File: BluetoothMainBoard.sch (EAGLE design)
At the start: 33 parts, among them IC1 MCP73831, J1 J_USB_MICROAB_HIROSE_ZX62-AB-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, U1 MAX921MSA/PR

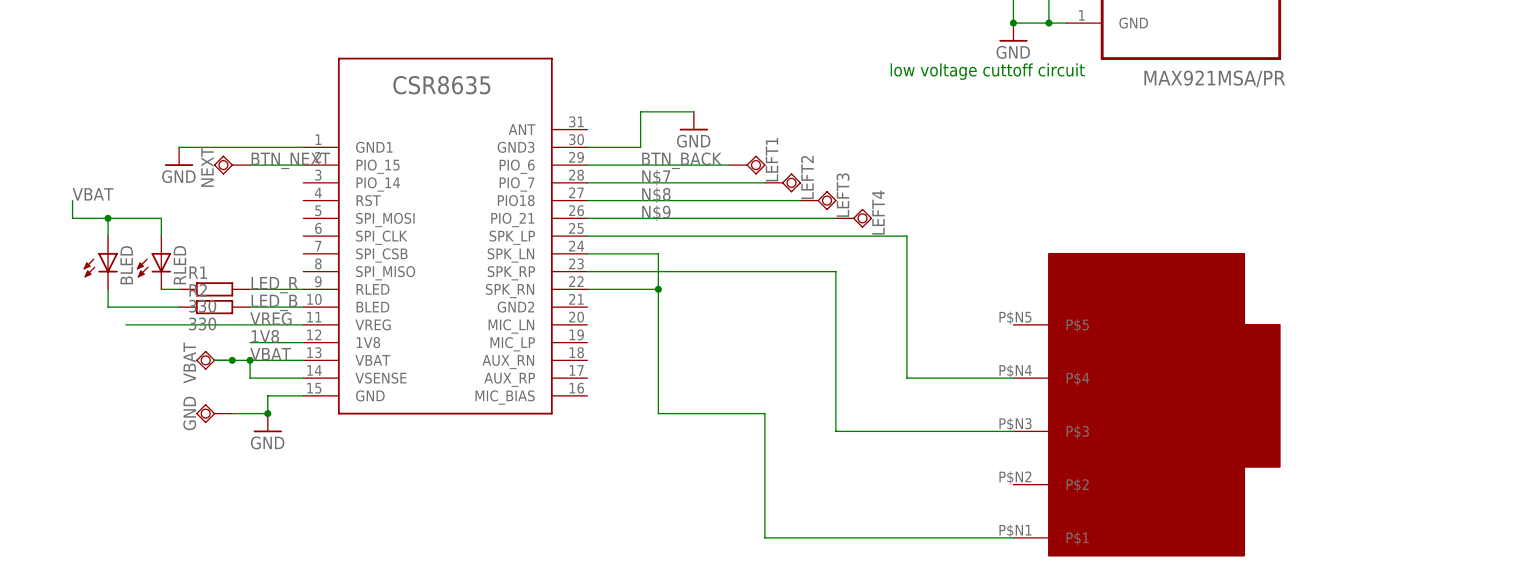
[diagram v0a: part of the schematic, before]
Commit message: Added buttons to the schematic. changed the wire labels
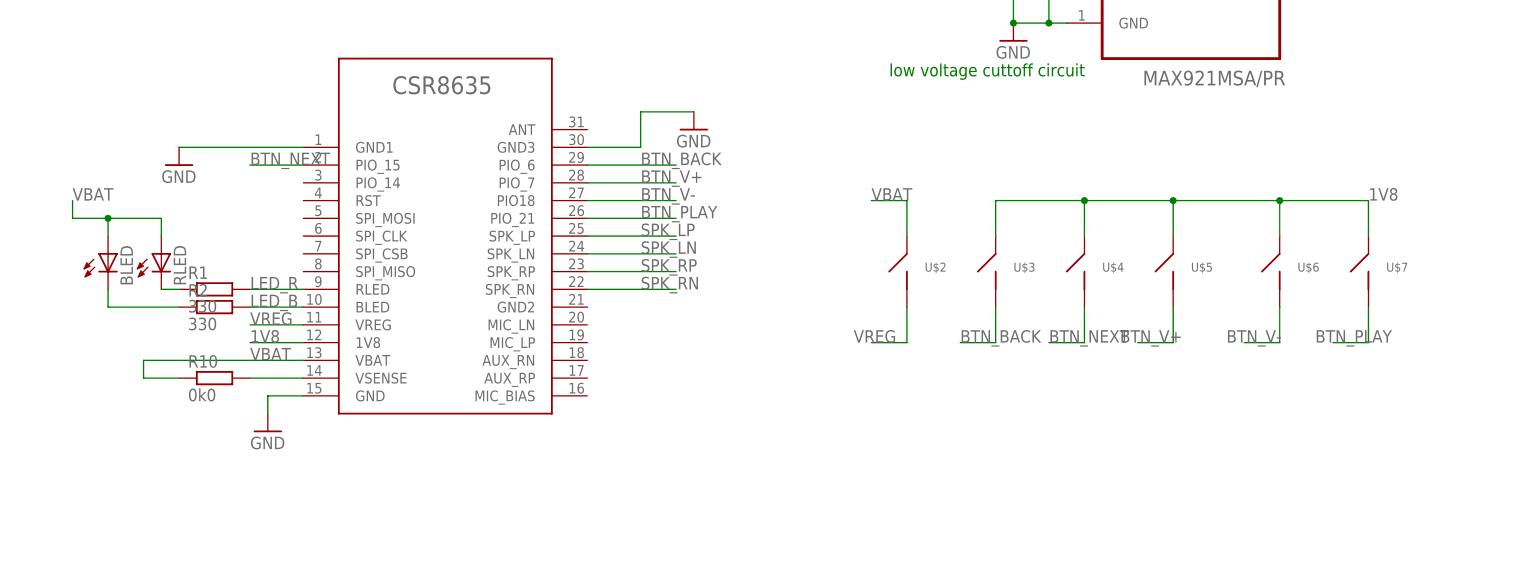
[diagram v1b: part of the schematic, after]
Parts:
- removed GND, LEFT1, LEFT2, LEFT3, LEFT4, NEXT, VBAT: TPSQB2,54, testpad:TPSQB2,54
- added R10: 0k0, rcl:R-EU_R0805W
- added U$3, U$4, U$5, U$6, U$7: TACTILE, Communica:TACTILE
- BLED, RLED: device led:LEDCHIP-LED0805 -> adafruit:LEDCHIPLED_1206
- U$2: value K3610 -> TACTILE; device CSR8635:K3610 -> Communica:TACTILE
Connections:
- removed net N$10: U$1.SPK_RP, U$2.P$3
- removed net N$4: U$1.SPK_LN, U$1.SPK_RN, U$2.P$1
- removed net N$7: LEFT2.TP, U$1.PIO_7
- removed net N$8: LEFT3.TP, U$1.PIO18
- removed net N$9: LEFT4.TP, U$1.PIO_21
- new net BTN_PLAY: U$1.PIO_21, U$7.P$2
- new net BTN_V+: U$1.PIO_7, U$5.P$2
- new net BTN_V-: U$1.PIO18, U$6.P$2
- new net SPK_LN: U$1.SPK_LN
- new net SPK_LP: U$1.SPK_LP
- new net SPK_RN: U$1.SPK_RN
- new net SPK_RP: U$1.SPK_RP
- net 1V8: now also U$3.P$1, U$4.P$1, U$5.P$1, U$6.P$1, U$7.P$1
- net BTN_BACK: now also U$3.P$2; no longer LEFT1.TP
- net BTN_NEXT: now also U$4.P$2; no longer NEXT.TP
- net GND: no longer GND.TP
- net N$2: now also R10.2, U$1.VSENSE; no longer U$1.SPK_LP, U$2.P$4
- net VBAT: now also R10.1, U$2.P$1; no longer U$1.VSENSE, VBAT.TP
- net VREG: now also U$2.P$2

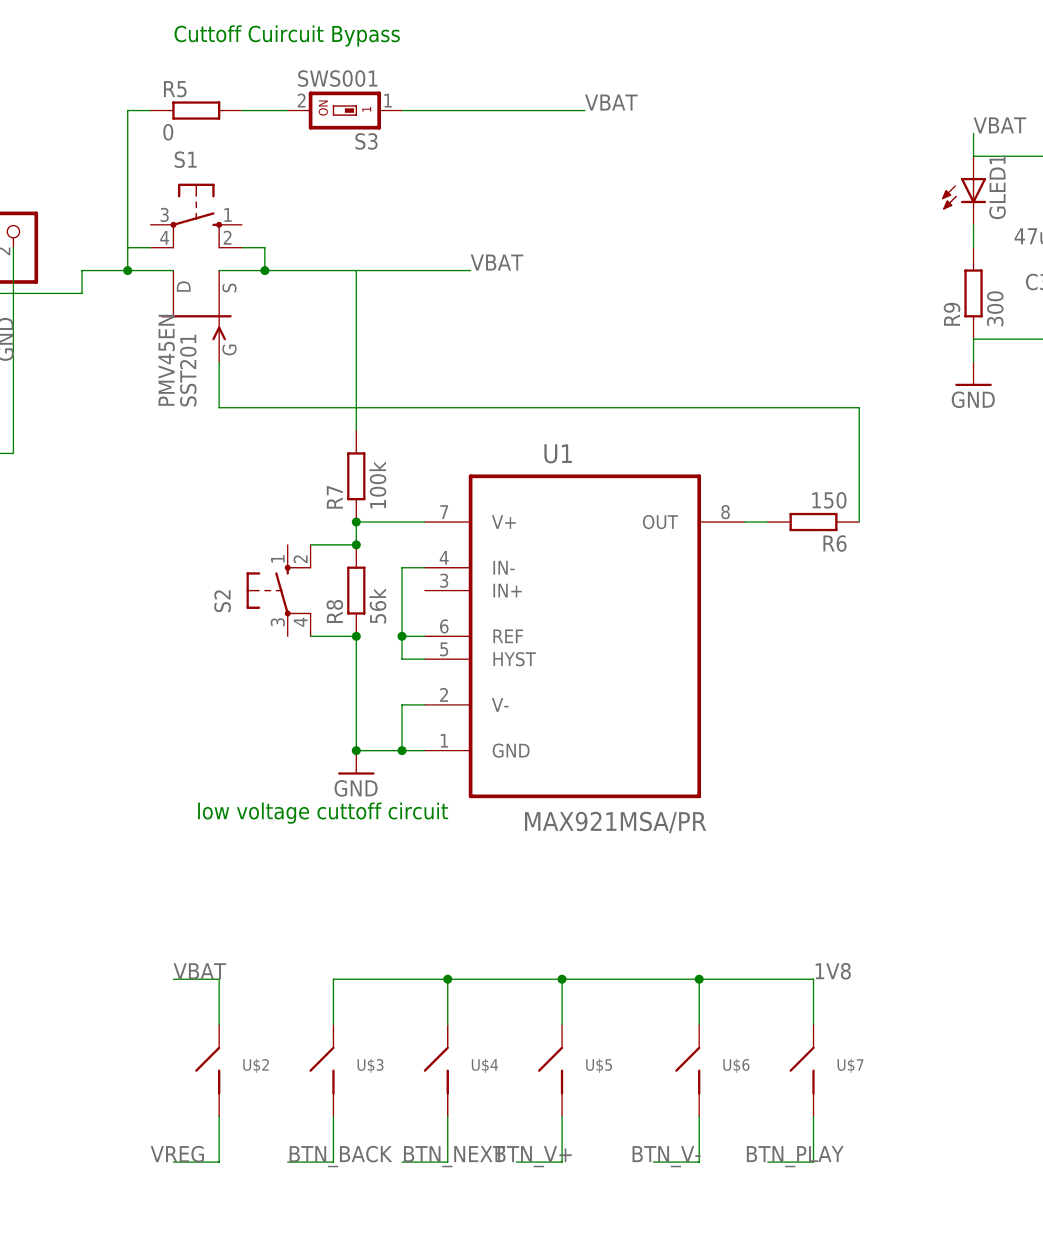
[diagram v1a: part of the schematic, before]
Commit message: changed resistor name
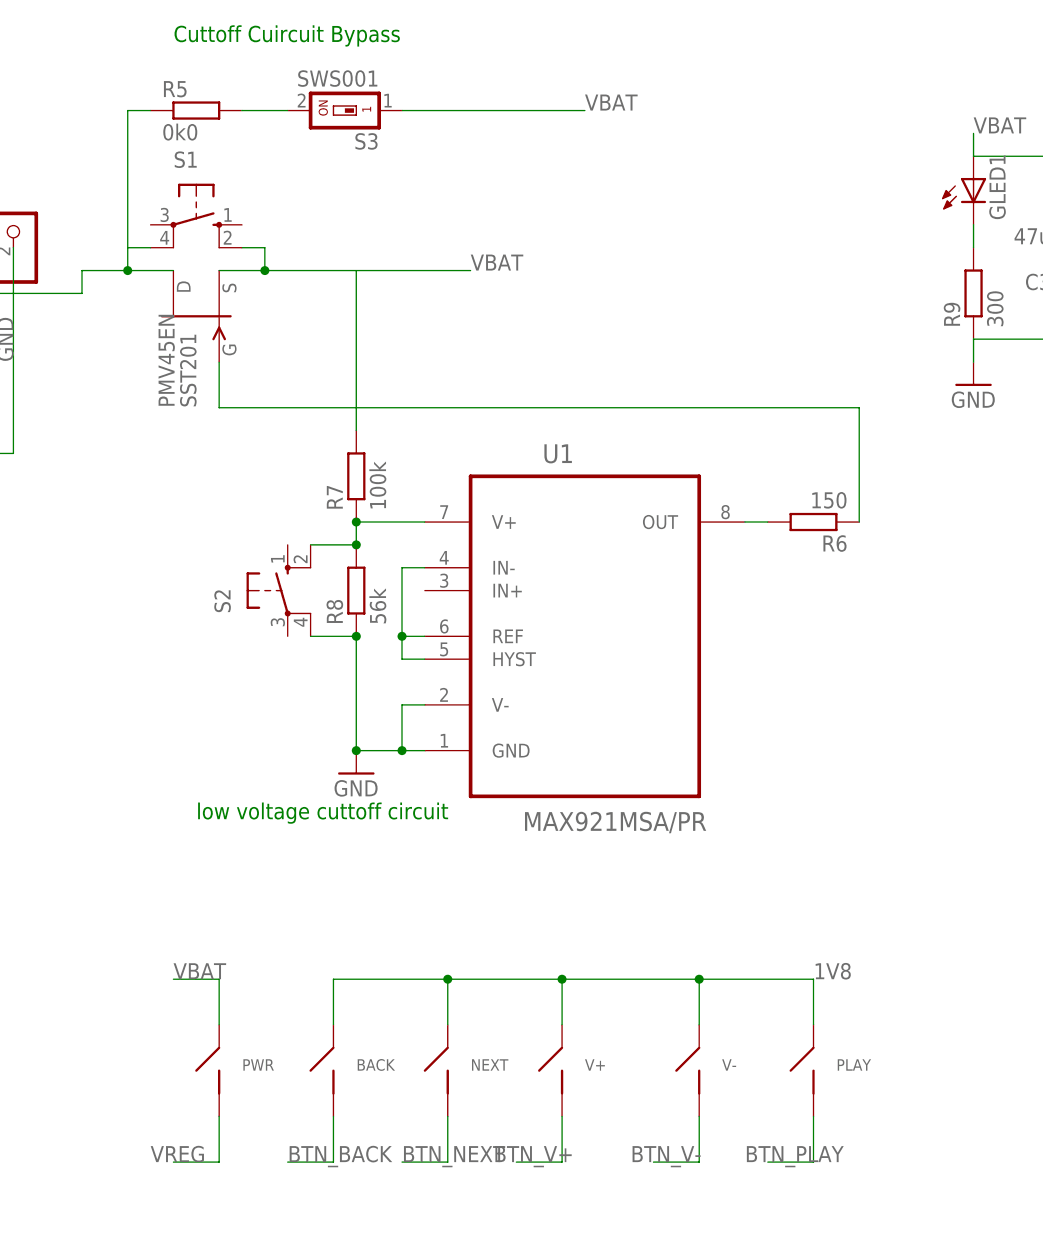
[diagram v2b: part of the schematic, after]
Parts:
- R5: value 0 -> 0k0
- renumbered U$2 to PWR, U$3 to BACK, U$4 to NEXT, U$5 to V+, U$6 to V-, U$7 to PLAY
